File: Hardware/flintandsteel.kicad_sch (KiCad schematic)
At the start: 47 parts, among them J1 RBUS, U1 ESP32-S3, U7 INA219AxDCN, Y1 R940000171

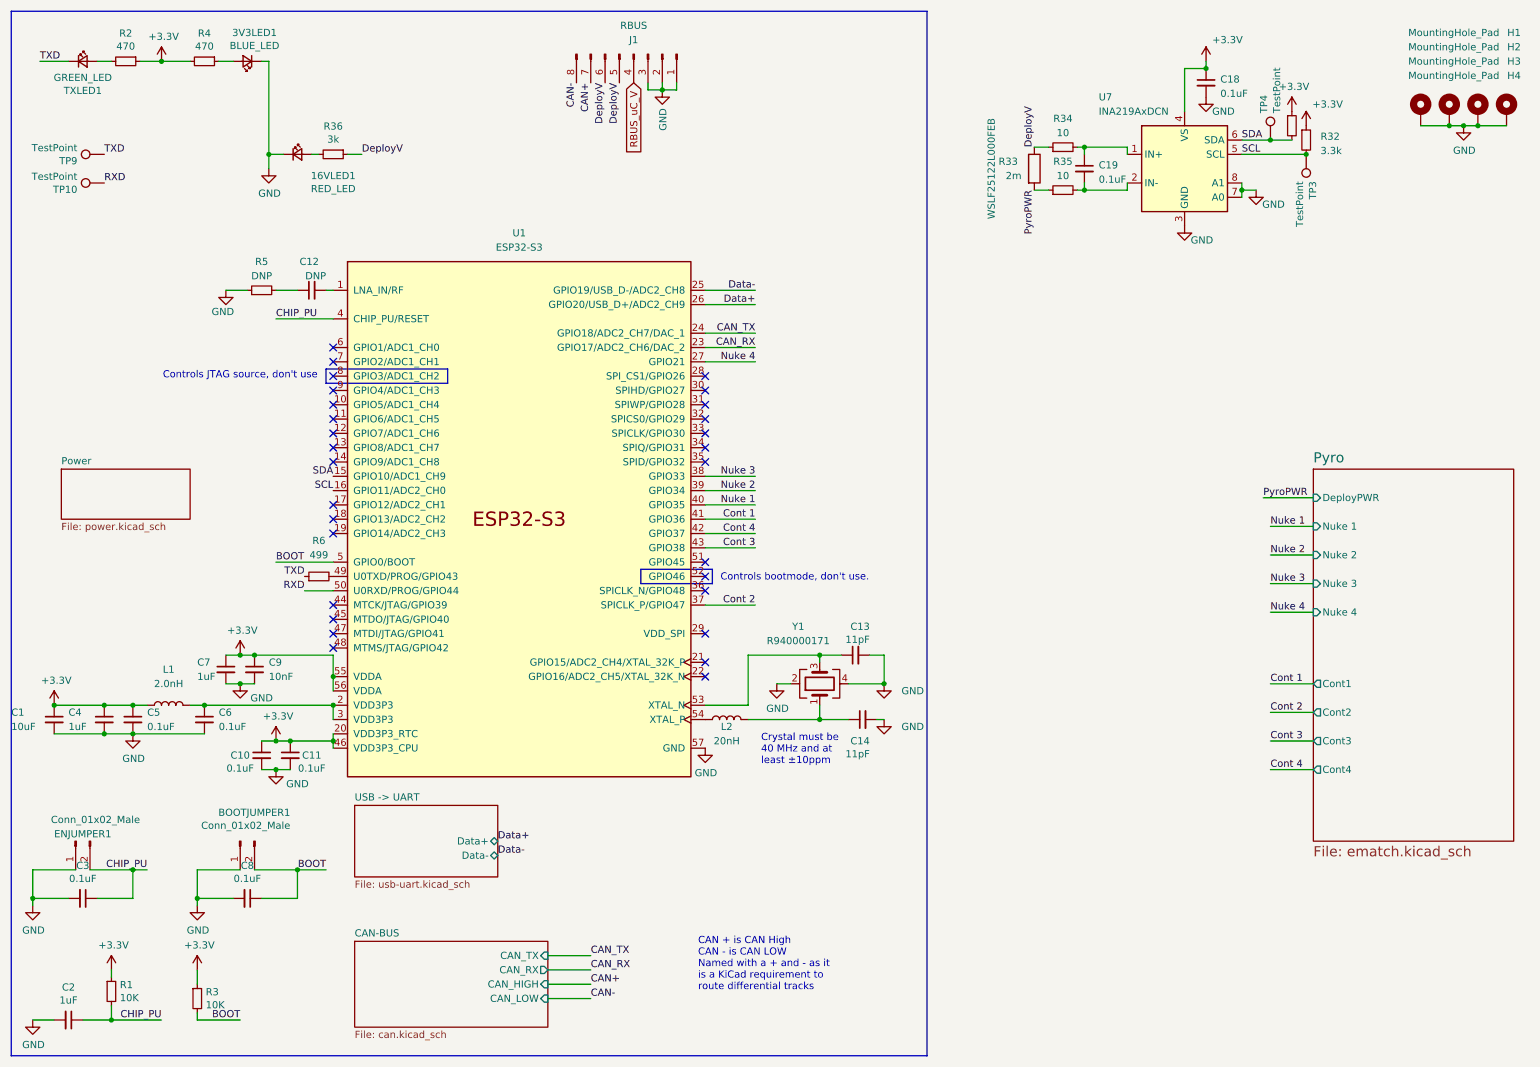
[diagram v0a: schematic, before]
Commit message: added high side switch
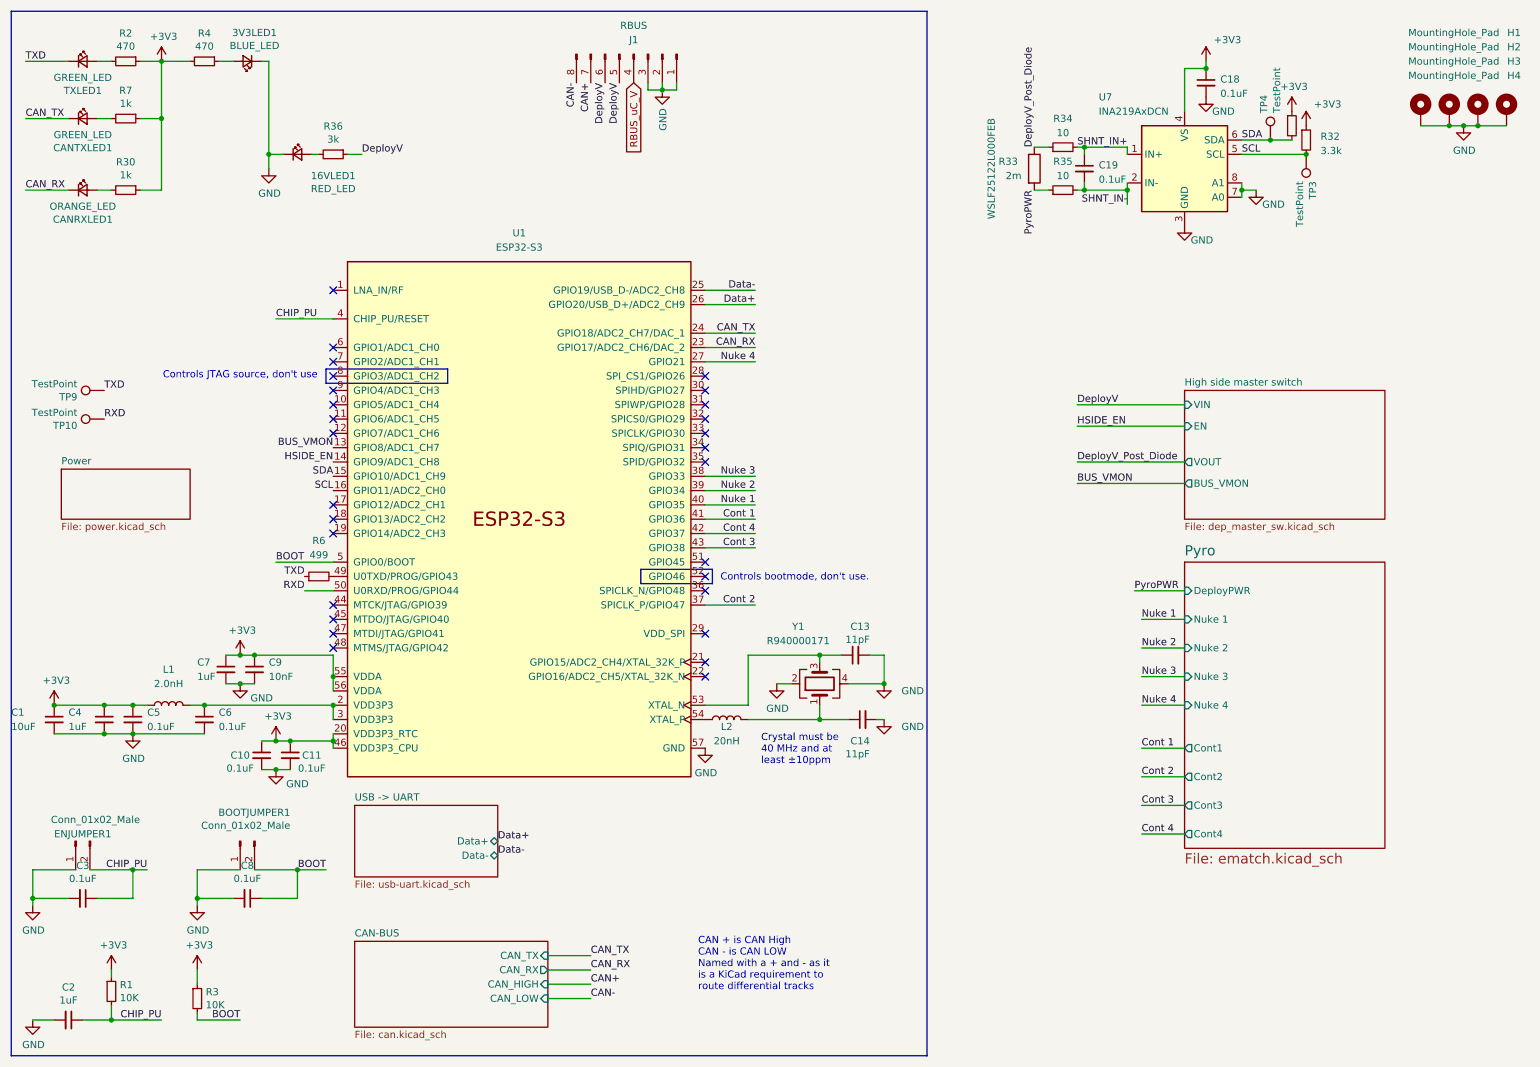
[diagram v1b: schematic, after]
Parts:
- removed C12: DNP, Capacitor_SMD:C_0402_1005Metric, symbol Device:C_Small
- removed R5: DNP, Resistor_SMD:R_0402_1005Metric, symbol Device:R_Small
- added CANRXLED1: ORANGE_LED, LED_SMD:LED_0402_1005Metric, symbol Device:LED_Small
- added CANTXLED1: GREEN_LED, LED_SMD:LED_0402_1005Metric, symbol Device:LED_Small
- added R30, R7: 1k, Resistor_SMD:R_0402_1005Metric, symbol Device:R_Small
- R33: MPN (none) -> WSLF25122L000FEB; Part Number WSLF25122L000FEB -> (none)
- R6: MPN (none) -> AC0402FR-07499RL
- Y1: footprint Crystal:Crystal_SMD_2016-4Pin_2.0x1.6mm -> iclr:Crystal_SMD_2016-4Pin_2.0x1.6mm
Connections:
- net +3V3: now also R30.1, R7.1
- net CAN_RX: now also CANRXLED1.1 (K)
- net CAN_TX: now also CANTXLED1.1 (K)
- net DeployV: no longer R33.1, R34.1
- net SHNT_IN-: now reaches C19.2, R35.2, U7.2 (IN-)
- net SHNT_IN+: now reaches C19.1, R34.2, U7.1 (IN+)
- net BUS_VMON: now reaches U1.13 (GPIO8/ADC1_CH7)
- net HSIDE_EN: now reaches U1.14 (GPIO9/ADC1_CH8)
- new net: CANRXLED1.2 (A), R30.2
- new net: CANTXLED1.2 (A), R7.2
- new net DeployV_Post_Diode: R33.1, R34.1
- no-connect marks 29 -> 28
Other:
- added sheet High side master switch (dep_master_sw.kicad_sch)
- moved on the sheet: TP10, TP9

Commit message: v3 hardware I guess
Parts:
- added 16VLED2: ORANGE_LED, LED_SMD:LED_0402_1005Metric, symbol Device:LED_Small
- added R40: 3k, Resistor_SMD:R_0402_1005Metric, symbol Device:R_Small
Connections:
- net Nuke 4 is gone; now on net Nuke 3: U1.27 (GPIO21)
- net Cont 1: now also U1.43 (GPIO38); no longer U1.41 (GPIO36)
- net Cont 3: now also U1.41 (GPIO36); no longer U1.43 (GPIO38)
- net GND: now also 16VLED2.1 (K)
- net Nuke 1: now also U1.39 (GPIO34); no longer U1.40 (GPIO35)
- net Nuke 2: now also U1.38 (GPIO33); no longer U1.39 (GPIO34)
- net Nuke 3: no longer U1.38 (GPIO33)
- net PyroPWR: now also R40.1
- net Cont 4 renamed Cont 0
- new net: 16VLED2.2 (A), R40.2
- new net Nuke 0: U1.40 (GPIO35)
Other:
- sheet Pyro ports: added Cont0, Nuke 0; removed Cont4, Nuke 4
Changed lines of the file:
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@@
 		(color 0 0 0 0)
 	)
+	(junction
+		(at 58.42 24.13)
+		(diameter 0)
+		(color 0 0 0 0)
+	)
 	(no_connect
 		(at 69.85 100.33)
@@
 	(wire
 		(pts
+			(xy 67.31 24.13) (xy 66.04 24.13)
+		)
+		(stroke
+			(width 0)
+			(type default)
+		)
+	)
+	(wire
+		(pts
 			(xy 30.48 191.77) (xy 30.48 189.23)
 		)
@@
 	(wire
 		(pts
+			(xy 58.42 24.13) (xy 60.96 24.13)
+		)
+		(stroke
+			(width 0)
+			(type default)
+		)
+	)
+	(wire
+		(pts
 			(xy 22.86 170.18) (xy 16.51 170.18)
 		)
@@
 	(wire
 		(pts
+			(xy 58.42 24.13) (xy 58.42 38.1)
+		)
+		(stroke
+			(width 0)
+			(type default)
+		)
+	)
+	(wire
+		(pts
 			(xy 213.36 143.51) (xy 220.98 143.51)
 		)
@@
 	(wire
 		(pts
+			(xy 74.93 24.13) (xy 72.39 24.13)
+		)
+		(stroke
+			(width 0)
+			(type default)
+		)
+	)
+	(wire
+		(pts
 			(xy 55.88 127) (xy 69.85 127)
 		)
@@
 	(wire
 		(pts
-			(xy 58.42 21.59) (xy 58.42 38.1)
+			(xy 58.42 21.59) (xy 58.42 24.13)
 		)
 		(stroke
@@
 		)
 	)
-	(label "Nuke 2"
+	(label "Nuke 1"
 		(at 213.36 125.73 0)
 		(fields_autoplaced yes)
@@
 		)
 	)
-	(label "Nuke 4"
+	(label "Nuke 3"
 		(at 144.78 74.93 180)
 		(fields_autoplaced yes)
@@
 		)
 	)
-	(label "Cont 1"
+	(label "Cont 0"
 		(at 213.36 143.51 0)
 		(fields_autoplaced yes)
@@
 		)
 	)
-	(label "Cont 2"
+	(label "Cont 1"
 		(at 213.36 148.59 0)
 		(fields_autoplaced yes)
@@
 		)
 	)
-	(label "Nuke 3"
+	(label "Nuke 2"
 		(at 213.36 130.81 0)
 		(fields_autoplaced yes)
@@
 		)
 	)
-	(label "Nuke 1"
+	(label "Nuke 0"
 		(at 144.78 100.33 180)
 		(fields_autoplaced yes)
@@
 		)
 	)
-	(label "Cont 4"
+	(label "Cont 0"
 		(at 144.78 105.41 180)
 		(fields_autoplaced yes)
@@
 		)
 	)
-	(label "Cont 4"
+	(label "Cont 3"
 		(at 213.36 158.75 0)
 		(fields_autoplaced yes)
@@
 		)
 	)
-	(label "Nuke 2"
+	(label "Nuke 1"
 		(at 144.78 97.79 180)
 		(fields_autoplaced yes)
@@
 		)
 	)
-	(label "Nuke 4"
+	(label "Nuke 3"
 		(at 213.36 135.89 0)
 		(fields_autoplaced yes)
@@
 		)
 	)
-	(label "Nuke 1"
+	(label "Nuke 0"
 		(at 213.36 120.65 0)
 		(fields_autoplaced yes)
@@
 		)
 	)
-	(label "Nuke 3"
+	(label "Nuke 2"
 		(at 144.78 95.25 180)
 		(fields_autoplaced yes)
@@
 		)
 	)
-	(label "Cont 3"
+	(label "Cont 2"
 		(at 213.36 153.67 0)
 		(fields_autoplaced yes)
@@
 		)
 	)
+	(label "PyroPWR"
+		(at 74.93 24.13 0)
+		(fields_autoplaced yes)
+		(effects
+			(font
+				(size 1.27 1.27)
+			)
+			(justify left bottom)
+		)
+	)
 	(label "CHIP_PU"
 		(at 59.69 67.31 0)
@@
 		)
 	)
-	(label "Cont 1"
+	(label "Cont 3"
 		(at 144.78 102.87 180)
 		(fields_autoplaced yes)
@@
 		)
 	)
-	(label "Cont 3"
+	(label "Cont 1"
 		(at 144.78 107.95 180)
 		(fields_autoplaced yes)
@@
 	)
 	(symbol
+		(lib_id "Device:LED_Small")
+		(at 63.5 24.13 0)
+		(unit 1)
+		(exclude_from_sim no)
+		(in_bom yes)
+		(on_board yes)
+		(dnp no)
+		(property "Reference" "16VLED2"
+			(at 69.85 27.94 0)
+			(effects
+				(font
+					(size 1.27 1.27)
+				)
+			)
+		)
+		(property "Value" "ORANGE_LED"
+			(at 69.85 30.2514 0)
+			(effects
+				(font
+					(size 1.27 1.27)
+				)
+			)
+		)
+		(property "Footprint" "LED_SMD:LED_0402_1005Metric"
+			(at 63.5 24.13 90)
+			(effects
+				(font
+					(size 1.27 1.27)
+				)
+				(hide yes)
+			)
+		)
+		(property "Datasheet" "~"
+			(at 63.5 24.13 90)
+			(effects
+				(font
+					(size 1.27 1.27)
+				)
+				(hide yes)
+			)
+		)
+		(property "Description" ""
+			(at 63.5 24.13 0)
+			(effects
+				(font
+					(size 1.27 1.27)
+				)
+				(hide yes)
+			)
+		)
+		(pin "1"
+		)
+		(pin "2"
+		)
+		(instances
+			(project "flintandsteel"
+				(path "/7db990e4-92e1-4f99-b4d2-435bbec1ba83"
+					(reference "16VLED2")
+					(unit 1)
+				)
+			)
+		)
+	)
+	(symbol
 		(lib_id "power:GND")
 		(at 53.34 132.08 0)
@@
 	)
 	(symbol
+		(lib_id "Device:R_Small")
+		(at 69.85 24.13 270)
+		(unit 1)
+		(exclude_from_sim no)
+		(in_bom yes)
+		(on_board yes)
+		(dnp no)
+		(property "Reference" "R40"
+			(at 69.85 19.1516 90)
+			(effects
+				(font
+					(size 1.27 1.27)
+				)
+			)
+		)
+		(property "Value" "3k"
+			(at 69.85 21.463 90)
+			(effects
+				(font
+					(size 1.27 1.27)
+				)
+			)
+		)
+		(property "Footprint" "Resistor_SMD:R_0402_1005Metric"
+			(at 69.85 24.13 0)
+			(effects
+				(font
+					(size 1.27 1.27)
+				)
+				(hide yes)
+			)
+		)
+		(property "Datasheet" "~"
+			(at 69.85 24.13 0)
+			(effects
+				(font
+					(size 1.27 1.27)
+				)
+				(hide yes)
+			)
+		)
+		(property "Description" ""
+			(at 69.85 24.13 0)
+			(effects
+				(font
+					(size 1.27 1.27)
+				)
+				(hide yes)
+			)
+		)
+		(pin "1"
+		)
+		(pin "2"
+		)
+		(instances
+			(project "flintandsteel"
+				(path "/7db990e4-92e1-4f99-b4d2-435bbec1ba83"
+					(reference "R40")
+					(unit 1)
+				)
+			)
+		)
+	)
+	(symbol
 		(lib_id "Device:L")
 		(at 139.7 138.43 90)
@@
 			)
 		)
-		(pin "Nuke 3" input
+		(pin "Nuke 2" input
 			(at 220.98 130.81 180)
 			(effects
@@
 			)
 		)
-		(pin "Nuke 1" input
+		(pin "Nuke 0" input
 			(at 220.98 120.65 180)
 			(effects
@@
 			)
 		)
-		(pin "Nuke 4" input
+		(pin "Nuke 3" input
 			(at 220.98 135.89 180)
 			(effects
@@
 			)
 		)
-		(pin "Nuke 2" input
+		(pin "Nuke 1" input
 			(at 220.98 125.73 180)
 			(effects
@@
 			)
 		)
-		(pin "Cont1" output
+		(pin "Cont0" output
 			(at 220.98 143.51 180)
 			(effects
@@
 			)
 		)
-		(pin "Cont2" output
+		(pin "Cont1" output
 			(at 220.98 148.59 180)
 			(effects
@@
 			)
 		)
-		(pin "Cont4" output
+		(pin "Cont3" output
 			(at 220.98 158.75 180)
 			(effects
@@
 			)
 		)
-		(pin "Cont3" output
+		(pin "Cont2" output
 			(at 220.98 153.67 180)
 			(effects

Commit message: forgot teardrops
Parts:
- J1: footprint Connector_Molex:Molex_Mini-Fit_Jr_5569-08A2_2x04_P4.20mm_Horizontal -> iclr:Molex_Mini-Fit_Jr_5569-08A2_2x04_P4.20mm_Horizontal
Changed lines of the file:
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@@
 			)
 		)
-		(property "Footprint" "Connector_Molex:Molex_Mini-Fit_Jr_5569-08A2_2x04_P4.20mm_Horizontal"
+		(property "Footprint" "iclr:Molex_Mini-Fit_Jr_5569-08A2_2x04_P4.20mm_Horizontal"
 			(at 123.19 20.32 0)
 			(effects

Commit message: files
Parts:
- added R47: 10k, Resistor_SMD:R_0402_1005Metric, symbol Device:R_Small
- H4: footprint MountingHole:MountingHole_3.2mm_M3_DIN965 -> MountingHole:MountingHole_3.2mm_M3_DIN965_Pad
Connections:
- net GND: now also R47.1
- net PyroPWR: now also R47.2
- net GPIO5: now reaches U1.10 (GPIO5/ADC1_CH4)
- net GPIO6: now reaches U1.11 (GPIO6/ADC1_CH5)
- net GPIO7: now reaches U1.12 (GPIO7/ADC1_CH6)
- net GPIO1: now reaches U1.6 (GPIO1/ADC1_CH0)
- net GPIO2: now reaches U1.7 (GPIO2/ADC1_CH1)
- net GPIO4: now reaches U1.9 (GPIO4/ADC1_CH3)
- no-connect marks 28 -> 22
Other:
- added sheet GPIO (GPIO.kicad_sch)

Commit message: tidied up schematic and bom
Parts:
- C103: renamed from C3; value 0.1uF -> 100nF
- C105: renamed from C5; value 0.1uF -> 100nF
- C106: renamed from C6; value 0.1uF -> 100nF
- C108: renamed from C8; value 0.1uF -> 100nF
- C110: renamed from C10; value 0.1uF -> 100nF
- C111: renamed from C11; value 0.1uF -> 100nF
- C114: renamed from C19; value 0.1uF -> 100nF
- C115: renamed from C18; value 0.1uF -> 100nF
- D101: renamed from TXLED1; value GREEN_LED -> LED_GREEN
- D102: renamed from CANTXLED1; value GREEN_LED -> LED_GREEN
- D103: renamed from CANRXLED1; value ORANGE_LED -> LED_ORANGE
- D104: renamed from 3V3LED1; value BLUE_LED -> LED_BLUE
- D105: renamed from 16VLED2; value ORANGE_LED -> LED_ORANGE
- D106: renamed from 16VLED1; value RED_LED -> LED_RED
- H101: renamed from H1; now left out of the parts list
- H102: renamed from H2; now left out of the parts list
- H103: renamed from H3; now left out of the parts list
- H104: renamed from H4; now left out of the parts list
- L101: renamed from L1; value 2.0nH -> 2nH
- R101: renamed from R1; value 10K -> 10kΩ
- R102: renamed from R2; value 470 -> 470Ω
- R103: renamed from R7; value 1k -> 1kΩ
- R104: renamed from R30; value 1k -> 1kΩ
- R105: renamed from R3; value 10K -> 10kΩ
- R106: renamed from R4; value 470 -> 470Ω
- R107: renamed from R6; value 499 -> 499Ω
- R108: renamed from R40; value 3k -> 3kΩ
- R109: renamed from R36; value 3k -> 3kΩ
- R110: renamed from R33; value 2m -> 2mΩ
- R111: renamed from R47; value 10k -> 10kΩ
- R112: renamed from R34; value 10 -> 10Ω
- R113: renamed from R35; value 10 -> 10Ω
- R114: renamed from R31; value 3.3k -> 3.3kΩ
- R115: renamed from R32; value 3.3k -> 3.3kΩ
- TP101: renamed from TP9; now left out of the parts list
- TP102: renamed from TP10; now left out of the parts list
- TP103: renamed from TP4; now left out of the parts list
- TP104: renamed from TP3; now left out of the parts list
- Y101: renamed from Y1; value R940000171 -> 40MHz±10ppm; footprint iclr:Crystal_SMD_2016-4Pin_2.0x1.6mm -> Crystal:Crystal_SMD_2016-4Pin_2.0x1.6mm; MPN (none) -> R940000171
- renumbered C1 to C101, C2 to C102, C4 to C104, C7 to C107, C9 to C109, C13 to C112, C14 to C113, ENJUMPER1 to J101, BOOTJUMPER1 to J102, J1 to J103, L2 to L102, U1 to U101, U7 to U102
